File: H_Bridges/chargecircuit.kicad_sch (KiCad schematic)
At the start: 2 parts, among them U2 max1898eub42+T

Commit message: designed charge circuit
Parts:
- added C1, C2: 100nF, symbol Device:C
- added C3: 10uF, symbol Device:C
- added D10: UPS115UE3/TR7, Footprints:POWERMITE1_DO-216AA_MIS_MCH, symbol Device:D_Schottky
- added Q10: PMOS, Footprints:SOT65P210X110-3N, symbol Simulation_SPICE:PMOS
- added R11: 2.8k, symbol Device:R_US
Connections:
- net GND: now also U2.6 (RSTRT), C1.2, C3.2, R11.2
- net VDD: now reaches D5.2 (A), U2.1 (IN)
- net VDD: now also C2.1
- net at U2.10 (CS): now also Q10.3 (S)
- net at U2.4 (ISET): now also R11.1
- net at U2.5 (CT): now also C1.1
- net VCC: now reaches U2.7 (BATT)
- net VCC: now also C3.1, D10.1 (K)
- net at U2.9 (DRV): now also C2.2, Q10.2 (G)
- new net: D10.2 (A), Q10.1 (D)
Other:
- moved on the sheet: D5, U2

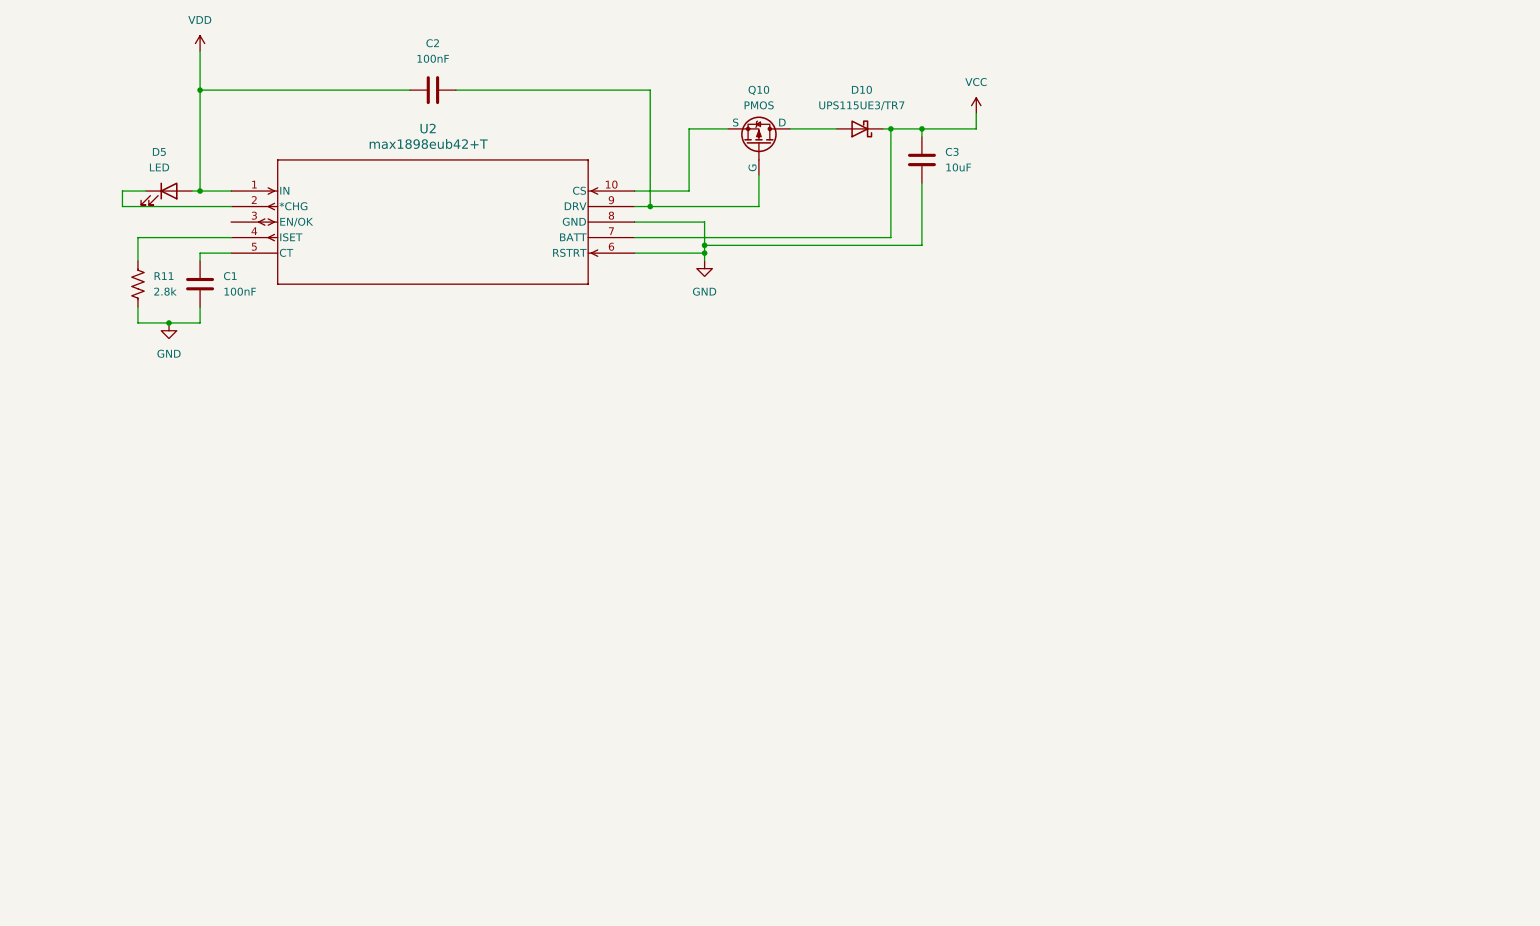
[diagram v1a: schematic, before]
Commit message: USB-C Input and Isolation Circuit
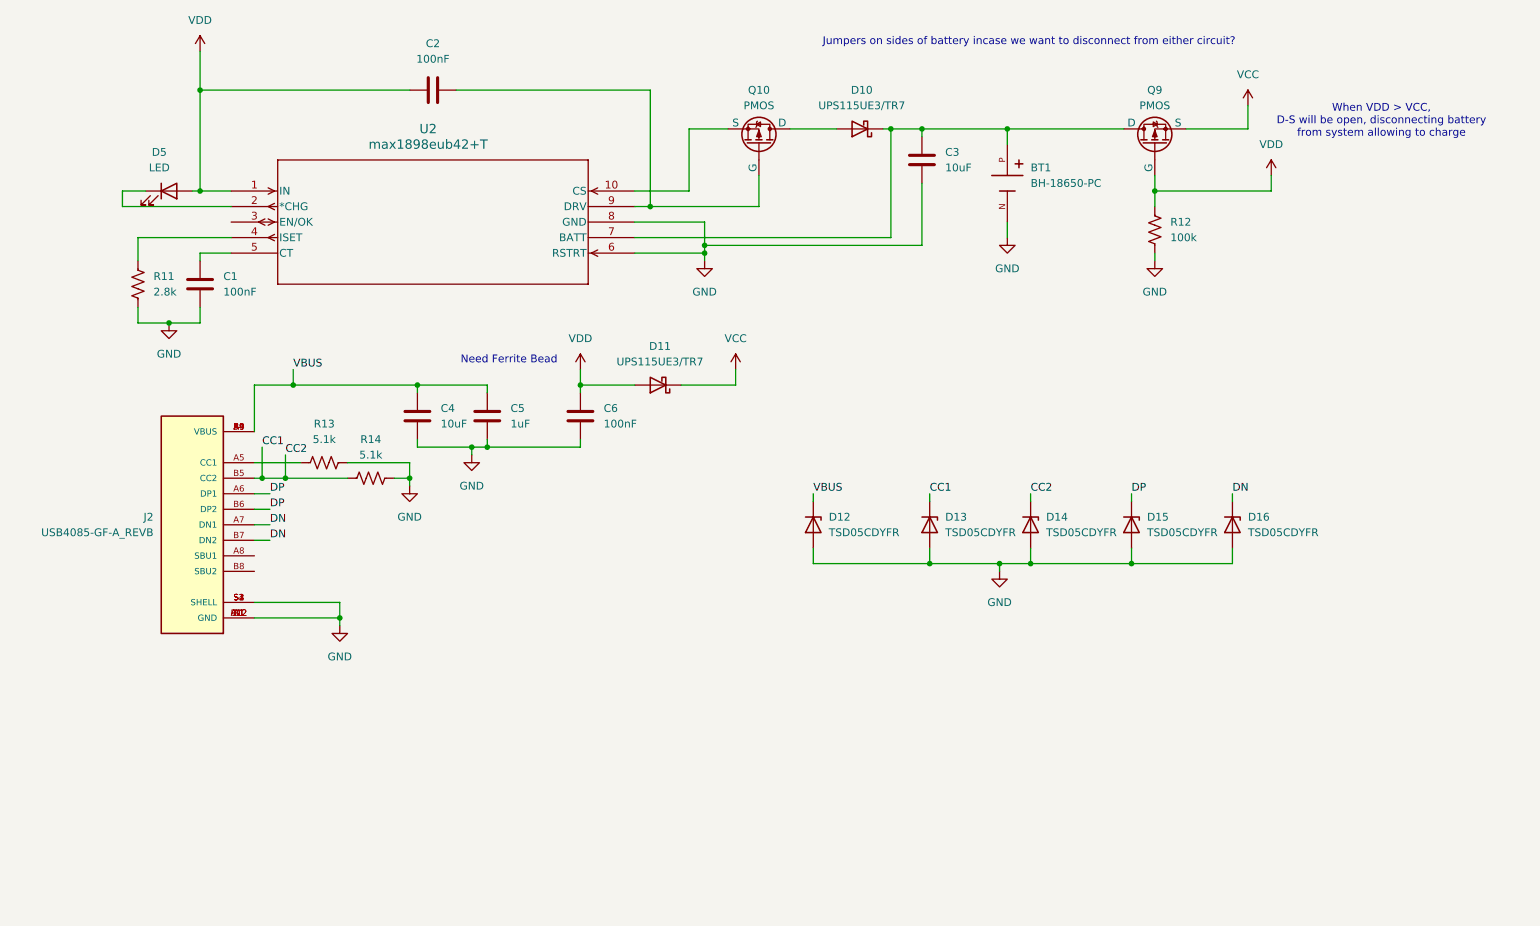
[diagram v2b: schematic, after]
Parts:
- added BT1: BH-18650-PC, Footprints:BAT_BH-18650-PC, symbol BH-18650-PC:BH-18650-PC
- added C4: 10uF, symbol Device:C
- added C5: 1uF, symbol Device:C
- added C6: 100nF, symbol Device:C
- added D11: UPS115UE3/TR7, Footprints:POWERMITE1_DO-216AA_MIS_MCH, symbol Device:D_Schottky
- added D12, D13, D14, D15, D16: TSD05CDYFR, Footprints:TVS_SOD2_DYF_TEX-L, symbol Diode:PTVS5V0Z1USK
- added J2: USB4085-GF-A_REVB, Footprints:GCT_USB4085-GF-A_REVB, symbol USB4085-GF-A_REVB:USB4085-GF-A_REVB
- added Q9: PMOS, Footprints:SOT65P210X110-3N, symbol Simulation_SPICE:PMOS
- added R12: 100k, symbol Device:R_US
- added R13, R14: 5.1k, symbol Device:R_US
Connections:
- net GND: now also BT1.N, C4.2, C5.2, C6.2, D12.2 (A), D13.2 (A), D14.2 (A), D15.2 (A), D16.2 (A), J2.A1 (GND), J2.A12 (GND), J2.B1 (GND), J2.B12 (GND), J2.S1 (SHELL), J2.S2 (SHELL), J2.S3 (SHELL), J2.S4 (SHELL), R12.2, R13.2, R14.2
- net VCC: now also D11.1 (K), Q9.3 (S); no longer C3.1, D10.1 (K), U2.7 (BATT)
- net VDD: now also C6.1, D11.2 (A), Q9.2 (G), R12.1
- new net: BT1.P, C3.1, D10.1 (K), Q9.1 (D), U2.7 (BATT)
- new net: J2.A5 (CC1), R13.1
- new net CC1: D13.1 (K), D14.1 (K), J2.B5 (CC2), R14.1
- new net DN: D16.1 (K), J2.A7 (DN1), J2.B7 (DN2)
- new net DP: D15.1 (K), J2.A6 (DP1), J2.B6 (DP2)
- new net VBUS: C4.1, C5.1, D12.1 (K), J2.A4 (VBUS), J2.A9 (VBUS), J2.B4 (VBUS), J2.B9 (VBUS)
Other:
- note added: "Jumpers on sides of battery incase we want to disconnect from either circuit?"
- note added: "Need Ferrite Bead"
- note added: "When VDD > VCC, D-S will be open, disconnecting battery from system allowing to charge"

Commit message: designed boost converter
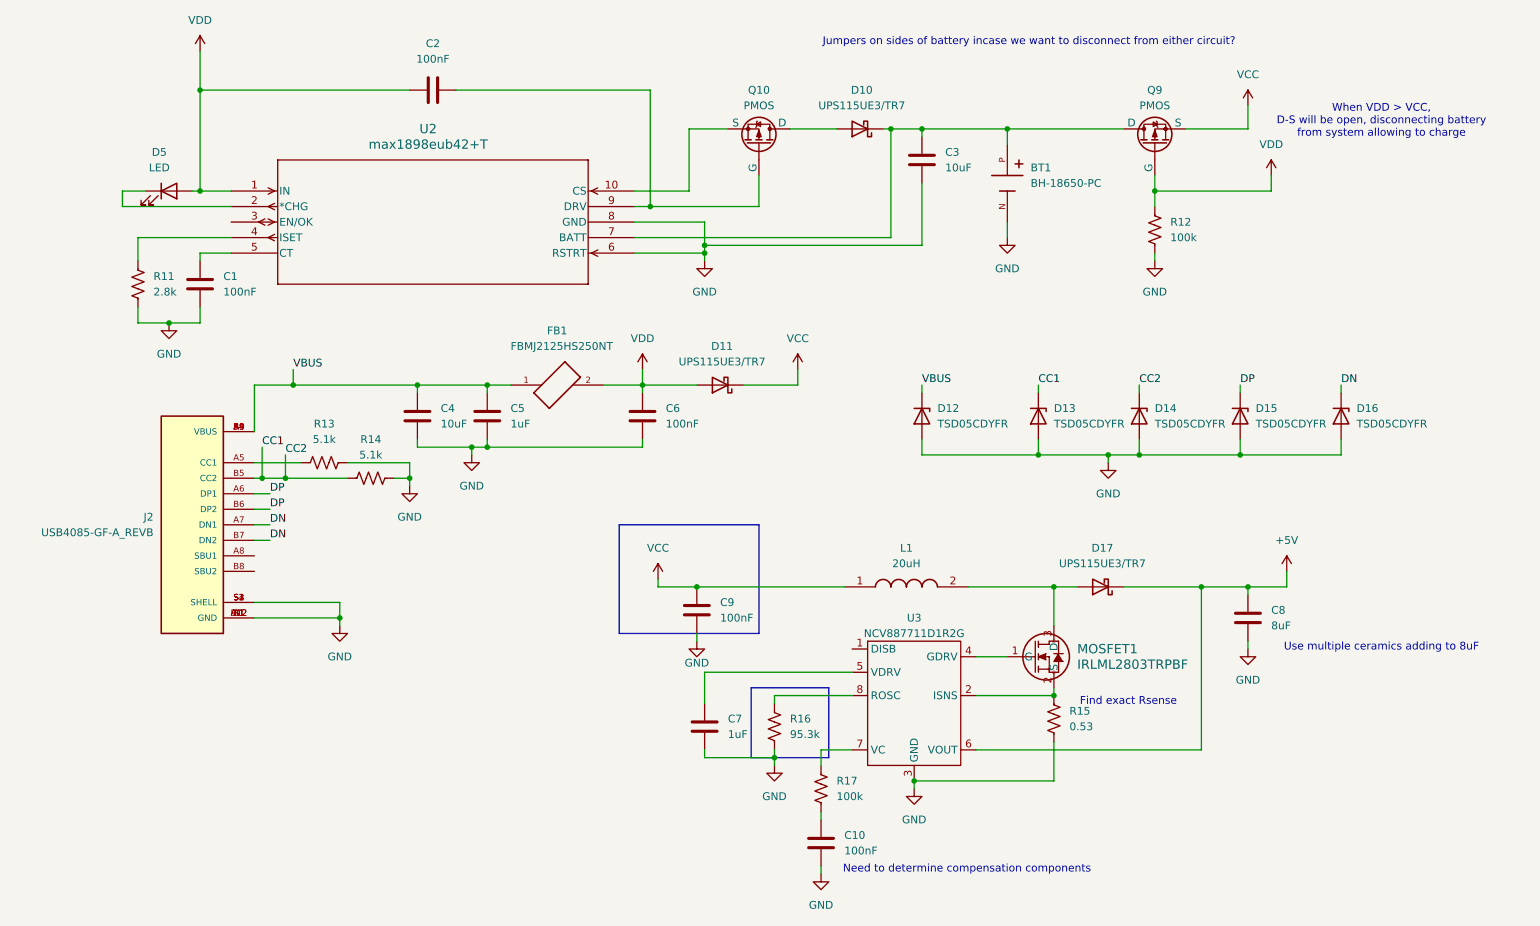
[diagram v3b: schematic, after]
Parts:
- added C10, C9: 100nF, symbol Device:C
- added C7: 1uF, symbol Device:C
- added C8: 8uF, symbol Device:C
- added D17: UPS115UE3/TR7, Footprints:POWERMITE1_DO-216AA_MIS_MCH, symbol Device:D_Schottky
- added FB1: FBMJ2125HS250NT, FBMJ2125HS250NT:BEADC2012X105N, symbol FBMJ2125HS250NT:FBMJ2125HS250NT
- added L1: 20uH, 7843332000, symbol 7843332000:7843332000
- added MOSFET1: IRLML2803TRPBF, MICRO3_SOT-23_INF, symbol IRLML2803TRPBF:IRLML2803TRPBF
- added R15: 0.53, symbol Device:R_US
- added R16: 95.3k, symbol Device:R_US
- added R17: 100k, symbol Device:R_US
- added U3: NCV887711D1R2G, Footprints:SOIC127P600X175-8N, symbol Hbridge_lib:NCV887711D1R2G
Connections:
- net GND: now also C10.2, C7.2, C8.2, C9.2, R15.2, R16.2, U3.3 (GND)
- net VBUS: now also FB1.1
- net VCC: now also C9.1, L1.1
- net VDD: now also FB1.2
- new net: R16.1, U3.8 (ROSC)
- new net: MOSFET1.2 (S), R15.1, U3.2 (ISNS)
- new net: R17.1, U3.7 (VC)
- new net: C10.1, R17.2
- new net: MOSFET1.1 (G), U3.4 (GDRV)
- new net: D17.2 (A), L1.2, MOSFET1.3 (D)
- new net: C7.1, U3.5 (VDRV)
- new net +5V: C8.1, D17.1 (K), U3.6 (VOUT)
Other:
- note added: "Find exact Rsense"
- note added: "Need to determine compensation components"
- note added: "Use multiple ceramics adding to 8uF"
- note removed: "Need Ferrite Bead"
- moved on the sheet: C6, D11, D12, D13, D14, D15, D16

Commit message: changed boost regulator
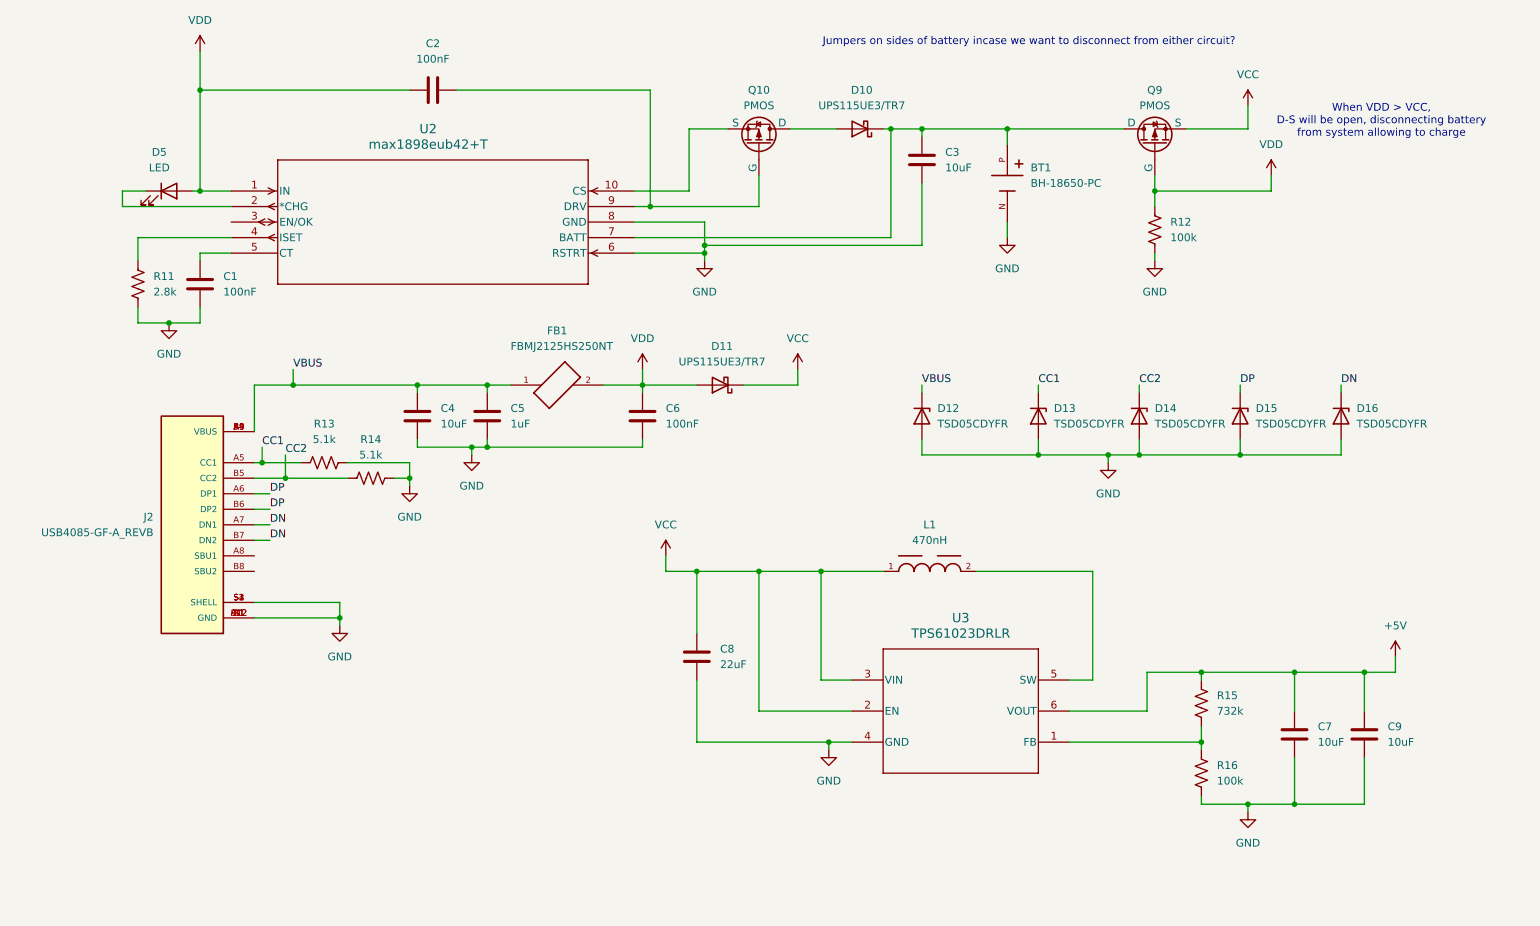
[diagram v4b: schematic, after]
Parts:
- removed C10: 100nF, symbol Device:C
- removed D17: UPS115UE3/TR7, Footprints:POWERMITE1_DO-216AA_MIS_MCH, symbol Device:D_Schottky
- removed L1: 20uH, 7843332000, symbol 7843332000:7843332000
- removed MOSFET1: IRLML2803TRPBF, MICRO3_SOT-23_INF, symbol IRLML2803TRPBF:IRLML2803TRPBF
- removed R17: 100k, symbol Device:R_US
- removed U3: NCV887711D1R2G, Footprints:SOIC127P600X175-8N, symbol Hbridge_lib:NCV887711D1R2G
- added L1: 470nH, WE-MAPI_3015:WE-MAPI_3015, symbol 744383350047:WE-MAPI_3015
- added U3: TPS61023DRLR, DRL0006A, symbol TPS61023DRLR:TPS61023DRLR
- C7: value 1uF -> 10uF
- C8: value 8uF -> 22uF
- C9: value 100nF -> 10uF
- R15: value 0.53 -> 732k
- R16: value 95.3k -> 100k
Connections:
- net +5V: now also C7.1, C9.1, R15.1, U3.6 (VOUT); no longer C8.1
- net CC1: now also J2.A5 (CC1), R13.1; no longer D14.1 (K), J2.B5 (CC2), R14.1
- net GND: now also U3.4 (GND); no longer R15.2
- net VCC: now also C8.1, L1.1, U3.2 (EN), U3.3 (VIN); no longer C9.1
- net at R16.1: now also R15.2, U3.1 (FB)
- new net: L1.2, U3.5 (SW)
- new net CC2: D14.1 (K), J2.B5 (CC2), R14.1
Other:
- note removed: "Find exact Rsense"
- note removed: "Need to determine compensation components"
- note removed: "Use multiple ceramics adding to 8uF"

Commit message: added resistor footprints
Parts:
- C1, C2, C3, C4, C5, C6, C7, C8, C9: footprint (none) -> Capacitor_SMD:C_0603_1608Metric
- R11, R12, R13, R14, R15, R16: footprint (none) -> Resistor_SMD:R_0603_1608Metric
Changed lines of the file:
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@@
 			)
 		)
-		(property "Footprint" ""
+		(property "Footprint" "Capacitor_SMD:C_0603_1608Metric"
 			(at 113.03 30.7848 0)
 			(effects
@@
 			)
 		)
-		(property "Footprint" ""
+		(property "Footprint" "Capacitor_SMD:C_0603_1608Metric"
 			(at 119.0752 88.9 0)
 			(effects
@@
 			)
 		)
-		(property "Footprint" ""
+		(property "Footprint" "Capacitor_SMD:C_0603_1608Metric"
 			(at 144.4752 88.9 0)
 			(effects
@@
 			)
 		)
-		(property "Footprint" ""
+		(property "Footprint" "Capacitor_SMD:C_0603_1608Metric"
 			(at 251.1552 140.97 0)
 			(effects
@@
 			)
 		)
-		(property "Footprint" ""
+		(property "Footprint" "Resistor_SMD:R_0603_1608Metric"
 			(at 235.966 132.334 90)
 			(effects
@@
 			)
 		)
-		(property "Footprint" ""
+		(property "Footprint" "Resistor_SMD:R_0603_1608Metric"
 			(at 91.694 91.694 90)
 			(effects
@@
 			)
 		)
-		(property "Footprint" ""
+		(property "Footprint" "Capacitor_SMD:C_0603_1608Metric"
 			(at 262.5852 140.97 0)
 			(effects
@@
 			)
 		)
-		(property "Footprint" ""
+		(property "Footprint" "Resistor_SMD:R_0603_1608Metric"
 			(at 99.314 94.234 90)
 			(effects
@@
 			)
 		)
-		(property "Footprint" ""
+		(property "Footprint" "Resistor_SMD:R_0603_1608Metric"
 			(at 235.966 143.764 90)
 			(effects
@@
 			)
 		)
-		(property "Footprint" ""
+		(property "Footprint" "Resistor_SMD:R_0603_1608Metric"
 			(at 228.346 54.864 90)
 			(effects
@@
 			)
 		)
-		(property "Footprint" ""
+		(property "Footprint" "Capacitor_SMD:C_0603_1608Metric"
 			(at 190.1952 46.99 0)
 			(effects
@@
 			)
 		)
-		(property "Footprint" ""
+		(property "Footprint" "Capacitor_SMD:C_0603_1608Metric"
 			(at 72.0852 67.31 0)
 			(effects
@@
 			)
 		)
-		(property "Footprint" ""
+		(property "Footprint" "Capacitor_SMD:C_0603_1608Metric"
 			(at 153.3652 128.27 0)
 			(effects
@@
 			)
 		)
-		(property "Footprint" ""
+		(property "Footprint" "Resistor_SMD:R_0603_1608Metric"
 			(at 61.976 63.754 90)
 			(effects
@@
 			)
 		)
-		(property "Footprint" ""
+		(property "Footprint" "Capacitor_SMD:C_0603_1608Metric"
 			(at 107.6452 88.9 0)
 			(effects

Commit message: exported Layout
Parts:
- D5: footprint (none) -> LED_SMD:LED_0402_1005Metric_Pad0.77x0.64mm_HandSolder
- FB1: footprint FBMJ2125HS250NT:BEADC2012X105N -> Footprints:BEADC2012X105N
- L1: footprint WE-MAPI_3015:WE-MAPI_3015 -> Footprints:WE-MAPI_3015
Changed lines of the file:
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@@
 			)
 		)
-		(property "Footprint" "FBMJ2125HS250NT:BEADC2012X105N"
+		(property "Footprint" "Footprints:BEADC2012X105N"
 			(at 129.54 80.01 0)
 			(effects
@@
 			)
 		)
-		(property "Footprint" "WE-MAPI_3015:WE-MAPI_3015"
+		(property "Footprint" "Footprints:WE-MAPI_3015"
 			(at 190.5 110.49 0)
 			(effects
@@
 			)
 		)
-		(property "Footprint" ""
+		(property "Footprint" "LED_SMD:LED_0402_1005Metric_Pad0.77x0.64mm_HandSolder"
 			(at 66.04 48.26 0)
 			(effects
